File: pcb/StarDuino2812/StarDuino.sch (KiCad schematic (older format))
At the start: 68 parts, among them J1 Screw_Terminal_01x02, Q1 IRLML6401, U1 ATmega328P-AU, Y1 Crystal

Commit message: 2812 star in work
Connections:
- net at U1.7 (XTAL1/PB6): now also C2.1, Y1.2
- net at U1.8 (XTAL2/PB7): now also C1.1, Y1.1
- net at D1.2 (DOUT): now also D5.4 (DIN); no longer D2.4 (DIN)
- net at D1.4 (DIN): now also D10.2 (DOUT)
- net at D2.2 (DOUT): now also D6.4 (DIN); no longer D3.4 (DIN)
- net at D3.2 (DOUT): now also D7.4 (DIN); no longer D4.4 (DIN)
- net at D4.2 (DOUT): now also D8.4 (DIN)
- net at D9.2 (DOUT): no longer D10.4 (DIN)
- net at D9.4 (DIN): now also D5.2 (DOUT)
- net at D11.4 (DIN): now also D7.2 (DOUT); no longer D10.2 (DOUT)
- net at D11.2 (DOUT): now also D2.4 (DIN); no longer D12.4 (DIN)
- net at D12.2 (DOUT): now also D3.4 (DIN)
- net at D17.2 (DOUT): no longer D18.4 (DIN)
- net at D18.2 (DOUT): no longer D19.4 (DIN)
- net at D19.2 (DOUT): no longer D20.4 (DIN)
- net at D25.2 (DOUT): no longer D26.4 (DIN)
- net at D26.2 (DOUT): no longer D27.4 (DIN)
- net at D27.2 (DOUT): no longer D28.4 (DIN)
- net at D33.2 (DOUT): no longer D34.4 (DIN)
- net at D34.2 (DOUT): no longer D35.4 (DIN)
- net at D35.2 (DOUT): no longer D36.4 (DIN)
- net at D41.2 (DOUT): no longer D42.4 (DIN)
- net at D42.2 (DOUT): no longer D43.4 (DIN)
- net at D43.2 (DOUT): no longer D44.4 (DIN)
- net at D49.2 (DOUT): no longer D50.4 (DIN)
- net at D50.2 (DOUT): no longer D51.4 (DIN)
- net at D51.2 (DOUT): no longer D52.4 (DIN)
- net at D57.2 (DOUT): no longer D58.4 (DIN)
- net at D58.2 (DOUT): no longer D59.4 (DIN)
- net at D59.2 (DOUT): no longer D60.4 (DIN)
- net at D6.2 (DOUT): now also D10.4 (DIN); no longer D7.4 (DIN)
- net at D8.2 (DOUT): now also D12.4 (DIN)
- net at D13.2 (DOUT): no longer D14.4 (DIN)
- net at D14.2 (DOUT): no longer D15.4 (DIN)
- net at D15.2 (DOUT): no longer D16.4 (DIN)
- net at D21.2 (DOUT): no longer D22.4 (DIN)
- net at D22.2 (DOUT): no longer D23.4 (DIN)
- net at D23.2 (DOUT): no longer D24.4 (DIN)
- net at D29.2 (DOUT): no longer D30.4 (DIN)
- net at D30.2 (DOUT): no longer D31.4 (DIN)
- net at D31.2 (DOUT): no longer D32.4 (DIN)
- net at D37.2 (DOUT): no longer D38.4 (DIN)
- net at D38.2 (DOUT): no longer D39.4 (DIN)
- net at D39.2 (DOUT): no longer D40.4 (DIN)
- net at D45.2 (DOUT): no longer D46.4 (DIN)
- net at D46.2 (DOUT): no longer D47.4 (DIN)
- net at D47.2 (DOUT): no longer D48.4 (DIN)
- net at D53.2 (DOUT): no longer D54.4 (DIN)
- net at D54.2 (DOUT): no longer D55.4 (DIN)
- net at D55.2 (DOUT): no longer D56.4 (DIN)
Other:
- moved on the sheet: D1, D10, D11, D12, D13, D14, D15, D16, D17, D18, D19, D2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

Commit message: 2812 star in work
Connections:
- net at D9.2 (DOUT): now also D16.4 (DIN)
- net at D17.2 (DOUT): now also D21.4 (DIN)
- net at D17.4 (DIN): now also D13.2 (DOUT)
- net at D18.2 (DOUT): now also D22.4 (DIN)
- net at D18.4 (DIN): now also D14.2 (DOUT)
- net at D19.2 (DOUT): now also D23.4 (DIN)
- net at D19.4 (DIN): now also D15.2 (DOUT)
- net at D20.2 (DOUT): now also D24.4 (DIN)
- net at D20.4 (DIN): now also D16.2 (DOUT)
- net at D25.2 (DOUT): now also D29.4 (DIN)
- net at D25.4 (DIN): now also D34.2 (DOUT)
- net at D26.2 (DOUT): now also D30.4 (DIN)
- net at D26.4 (DIN): now also D35.2 (DOUT)
- net at D27.2 (DOUT): now also D31.4 (DIN)
- net at D27.4 (DIN): now also D36.2 (DOUT)
- net at D28.2 (DOUT): now also D32.4 (DIN)
- net at D28.4 (DIN): now also D21.2 (DOUT)
- net at D33.2 (DOUT): now also D40.4 (DIN)
- net at D33.4 (DIN): now also D29.2 (DOUT)
- net at D34.4 (DIN): now also D30.2 (DOUT)
- net at D35.4 (DIN): now also D31.2 (DOUT)
- net at D36.4 (DIN): now also D32.2 (DOUT)
- net at D41.2 (DOUT): now also D45.4 (DIN)
- net at D41.4 (DIN): now also D37.2 (DOUT)
- net at D42.2 (DOUT): now also D46.4 (DIN)
- net at D42.4 (DIN): now also D38.2 (DOUT)
- net at D43.2 (DOUT): now also D47.4 (DIN)
- net at D43.4 (DIN): now also D39.2 (DOUT)
- net at D44.2 (DOUT): now also D48.4 (DIN)
- net at D44.4 (DIN): now also D40.2 (DOUT)
- net at D49.2 (DOUT): now also D53.4 (DIN)
- net at D49.4 (DIN): now also D58.2 (DOUT)
- net at D50.2 (DOUT): now also D54.4 (DIN)
- net at D50.4 (DIN): now also D59.2 (DOUT)
- net at D51.2 (DOUT): now also D55.4 (DIN)
- net at D51.4 (DIN): now also D60.2 (DOUT)
- net at D52.2 (DOUT): now also D56.4 (DIN)
- net at D52.4 (DIN): now also D45.2 (DOUT)
- net at D57.4 (DIN): now also D53.2 (DOUT)
- net at D58.4 (DIN): now also D54.2 (DOUT)
- net at D59.4 (DIN): now also D55.2 (DOUT)
- net at D60.4 (DIN): now also D56.2 (DOUT)
- net at D13.4 (DIN): now also D22.2 (DOUT)
- net at D14.4 (DIN): now also D23.2 (DOUT)
- net at D15.4 (DIN): now also D24.2 (DOUT)
- net at D37.4 (DIN): now also D46.2 (DOUT)
- net at D38.4 (DIN): now also D47.2 (DOUT)
- net at D39.4 (DIN): now also D48.2 (DOUT)
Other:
- moved on the sheet: H1

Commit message: Almost ready
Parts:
- added C4: 0.1uF, Capacitor_SMD:C_0805_2012Metric_Pad1.18x1.45mm_HandSolder, symbol Device:C
- added H2, H3, H4: MountingHole, MountingHole:MountingHole_2.5mm, symbol Mechanical:MountingHole
- added J2: Conn_01x03_Male, Connector_PinHeader_2.54mm:PinHeader_1x03_P2.54mm_Vertical, symbol Connector:Conn_01x03_Male
- added R1: 1M, Resistor_SMD:R_0805_2012Metric_Pad1.20x1.40mm_HandSolder, symbol Device:R
- added R2: 10k, Resistor_SMD:R_0805_2012Metric_Pad1.20x1.40mm_HandSolder, symbol Device:R
- Y1: value Crystal -> 16M; footprint Crystal:Crystal_SMD_HC49-SD_HandSoldering -> Crystal:Crystal_HC49-4H_Vertical
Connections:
- net GND: now also C4.1
- net VCC: now also U1.18 (AVCC), U1.4 (VCC), U1.6 (VCC), C4.2, R2.1
- net at U1.24 (PC1): now also D4.4 (DIN)
- net ~Reset: now reaches U1.29 (~RESET~/PC6)
- net ~Reset: now also J2.1 (Pin_1), R2.2
- net RX: now reaches U1.30 (PD0)
- net RX: now also J2.2 (Pin_2)
- net TX: now reaches U1.31 (PD1)
- net TX: now also J2.3 (Pin_3)
- net at C2.1, U1.7 (XTAL1/PB6), Y1.2: now also R1.1
- net at C1.1, U1.8 (XTAL2/PB7), Y1.1: now also R1.2
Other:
- moved on the sheet: C1, C2

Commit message: Add fifth hole
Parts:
- added H5: MountingHole, MountingHole:MountingHole_2.5mm, symbol Mechanical:MountingHole
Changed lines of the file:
@@
 Wire Wire Line
 	3525 6250 3100 6250
+$Comp
+L Mechanical:MountingHole H5
+U 1 1 601A7A2A
+P 10850 7225
+F 0 "H5" H 10950 7271 50  0000 L CNN
+F 1 "MountingHole" H 10950 7180 50  0000 L CNN
+F 2 "MountingHole:MountingHole_2.5mm" H 10850 7225 50  0001 C CNN
+F 3 "~" H 10850 7225 50  0001 C CNN
+	1    10850 7225
+	1    0    0    -1
+$EndComp
 $EndSCHEMATC

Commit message: Replace Mounting holes to Mounting pads Add capacitor Add resistors to UART
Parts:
- removed H1, H2, H3, H4, H5: MountingHole, MountingHole:MountingHole_2.5mm, symbol Mechanical:MountingHole
- added C5: 0.1uF, Capacitor_SMD:C_0805_2012Metric_Pad1.18x1.45mm_HandSolder, symbol Device:C
- added C6: 470uF, Capacitor_THT:CP_Axial_L20.0mm_D10.0mm_P26.00mm_Horizontal, symbol Device:CP
- added H10, H6, H7, H8, H9: MountingHole_Pad, MountingHole:MountingHole_2.5mm_Pad_Via, symbol Mechanical:MountingHole_Pad
- added J3: Conn_01x01_Male, Connector_PinHeader_2.54mm:PinHeader_1x01_P2.54mm_Vertical, symbol Connector:Conn_01x01_Male
- added R3, R4: 1k, Resistor_SMD:R_0805_2012Metric_Pad1.20x1.40mm_HandSolder, symbol Device:R
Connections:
- net GND: now also C6.2, J3.1 (Pin_1)
- net RX: now also R3.2; no longer J2.2 (Pin_2)
- net TX: now also R4.2; no longer J2.3 (Pin_3)
- net VCC: now also C6.1
- net ~Reset: now also C5.2; no longer J2.1 (Pin_1)
- new net: C5.1, J2.1 (Pin_1)
- new net: J2.2 (Pin_2), R3.1
- new net: J2.3 (Pin_3), R4.1
- no-connect marks 0 -> 26
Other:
- moved on the sheet: J2
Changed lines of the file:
@@
 Reverse\npolarity\nprotection
-$Comp
-L Mechanical:MountingHole H1
-U 1 1 6027D2D2
-P 10850 5575
-F 0 "H1" H 10950 5621 50  0000 L CNN
-F 1 "MountingHole" H 10950 5530 50  0000 L CNN
-F 2 "MountingHole:MountingHole_2.5mm" H 10850 5575 50  0001 C CNN
-F 3 "~" H 10850 5575 50  0001 C CNN
-	1    10850 5575
-	1    0    0    -1
-$EndComp
 $Comp
 L power:VCC #PWR097
@@
 Wire Wire Line
 	5000 16000 5000 16750
-$Comp
-L Mechanical:MountingHole H2
-U 1 1 60124CA1
-P 10850 5975
-F 0 "H2" H 10950 6021 50  0000 L CNN
-F 1 "MountingHole" H 10950 5930 50  0000 L CNN
-F 2 "MountingHole:MountingHole_2.5mm" H 10850 5975 50  0001 C CNN
-F 3 "~" H 10850 5975 50  0001 C CNN
-	1    10850 5975
-	1    0    0    -1
-$EndComp
-$Comp
-L Mechanical:MountingHole H3
-U 1 1 60125FF8
-P 10850 6375
-F 0 "H3" H 10950 6421 50  0000 L CNN
-F 1 "MountingHole" H 10950 6330 50  0000 L CNN
-F 2 "MountingHole:MountingHole_2.5mm" H 10850 6375 50  0001 C CNN
-F 3 "~" H 10850 6375 50  0001 C CNN
-	1    10850 6375
-	1    0    0    -1
-$EndComp
-$Comp
-L Mechanical:MountingHole H4
-U 1 1 601346AF
-P 10850 6800
-F 0 "H4" H 10950 6846 50  0000 L CNN
-F 1 "MountingHole" H 10950 6755 50  0000 L CNN
-F 2 "MountingHole:MountingHole_2.5mm" H 10850 6800 50  0001 C CNN
-F 3 "~" H 10850 6800 50  0001 C CNN
-	1    10850 6800
-	1    0    0    -1
-$EndComp
 Wire Wire Line
 	2950 4950 3250 4950
@@
 Text Label 3275 6050 0    50   ~ 0
 ~Reset
-Wire Wire Line
-	3200 6050 3525 6050
 Text Label 3275 6150 0    50   ~ 0
 RX
@@
 L Connector:Conn_01x03_Male J2
 U 1 1 60414868
-P 3725 6150
-F 0 "J2" H 3697 6174 50  0000 R CNN
-F 1 "Conn_01x03_Male" H 3697 6083 50  0000 R CNN
-F 2 "Connector_PinHeader_2.54mm:PinHeader_1x03_P2.54mm_Vertical" H 3725 6150 50  0001 C CNN
-F 3 "~" H 3725 6150 50  0001 C CNN
-	1    3725 6150
+P 4350 6150
+F 0 "J2" H 4322 6174 50  0000 R CNN
+F 1 "Conn_01x03_Male" H 4675 5950 50  0000 R CNN
+F 2 "Connector_PinHeader_2.54mm:PinHeader_1x03_P2.54mm_Vertical" H 4350 6150 50  0001 C CNN
+F 3 "~" H 4350 6150 50  0001 C CNN
+	1    4350 6150
 	-1   0    0    -1
 $EndComp
@@
 	3525 6250 3100 6250
 $Comp
-L Mechanical:MountingHole H5
-U 1 1 601A7A2A
-P 10850 7225
-F 0 "H5" H 10950 7271 50  0000 L CNN
-F 1 "MountingHole" H 10950 7180 50  0000 L CNN
-F 2 "MountingHole:MountingHole_2.5mm" H 10850 7225 50  0001 C CNN
-F 3 "~" H 10850 7225 50  0001 C CNN
-	1    10850 7225
-	1    0    0    -1
-$EndComp
+L Device:R R4
+U 1 1 606499DB
+P 3675 6250
+F 0 "R4" V 3625 6075 50  0000 C CNN
+F 1 "1k" V 3675 6250 50  0000 C CNN
+F 2 "Resistor_SMD:R_0805_2012Metric_Pad1.20x1.40mm_HandSolder" V 3605 6250 50  0001 C CNN
+F 3 "~" H 3675 6250 50  0001 C CNN
+	1    3675 6250
+	0    1    1    0
+$EndComp
+$Comp
+L Device:R R3
+U 1 1 6064AD4D
+P 3675 6150
+F 0 "R3" V 3625 5975 50  0000 C CNN
+F 1 "1k" V 3675 6150 50  0000 C CNN
+F 2 "Resistor_SMD:R_0805_2012Metric_Pad1.20x1.40mm_HandSolder" V 3605 6150 50  0001 C CNN
+F 3 "~" H 3675 6150 50  0001 C CNN
+	1    3675 6150
+	0    1    1    0
+$EndComp
+$Comp
+L Device:C C5
+U 1 1 6064C37E
+P 3875 6050
+F 0 "C5" V 3825 5950 50  0000 C CNN
+F 1 "0.1uF" V 3825 6225 50  0000 C CNN
+F 2 "Capacitor_SMD:C_0805_2012Metric_Pad1.18x1.45mm_HandSolder" H 3913 5900 50  0001 C CNN
+F 3 "~" H 3875 6050 50  0001 C CNN
+	1    3875 6050
+	0    1    1    0
+$EndComp
+Wire Wire Line
+	3200 6050 3725 6050
+Wire Wire Line
+	3825 6150 4150 6150
+Wire Wire Line
+	3825 6250 4150 6250
+Wire Wire Line
+	4025 6050 4150 6050
+NoConn ~ 1750 4250
+NoConn ~ 1750 4450
+NoConn ~ 1750 4550
+NoConn ~ 2950 4250
+NoConn ~ 2950 4350
+NoConn ~ 2950 4450
+NoConn ~ 2950 4550
+NoConn ~ 2950 4650
+NoConn ~ 2950 4750
+NoConn ~ 2950 5150
+NoConn ~ 2950 5350
+NoConn ~ 2950 5450
+NoConn ~ 2950 5550
+NoConn ~ 2950 5650
+NoConn ~ 2950 6150
+NoConn ~ 2950 6250
+NoConn ~ 2950 6350
+NoConn ~ 2950 6450
+NoConn ~ 2950 6550
+NoConn ~ 2950 6650
+NoConn ~ 9350 18750
+$Comp
+L Mechanical:MountingHole_Pad H6
+U 1 1 60810FD8
+P 12250 5550
+F 0 "H6" H 12350 5599 50  0000 L CNN
+F 1 "MountingHole_Pad" H 12350 5508 50  0000 L CNN
+F 2 "MountingHole:MountingHole_2.5mm_Pad_Via" H 12250 5550 50  0001 C CNN
+F 3 "~" H 12250 5550 50  0001 C CNN
+	1    12250 5550
+	1    0    0    -1
+$EndComp
+$Comp
+L Mechanical:MountingHole_Pad H7
+U 1 1 60812577
+P 12250 6050
+F 0 "H7" H 12350 6099 50  0000 L CNN
+F 1 "MountingHole_Pad" H 12350 6008 50  0000 L CNN
+F 2 "MountingHole:MountingHole_2.5mm_Pad_Via" H 12250 6050 50  0001 C CNN
+F 3 "~" H 12250 6050 50  0001 C CNN
+	1    12250 6050
+	1    0    0    -1
+$EndComp
+$Comp
+L Mechanical:MountingHole_Pad H8
+U 1 1 60812E0D
+P 12250 6550
+F 0 "H8" H 12350 6599 50  0000 L CNN
+F 1 "MountingHole_Pad" H 12350 6508 50  0000 L CNN
+F 2 "MountingHole:MountingHole_2.5mm_Pad_Via" H 12250 6550 50  0001 C CNN
+F 3 "~" H 12250 6550 50  0001 C CNN
+	1    12250 6550
+	1    0    0    -1
+$EndComp
+$Comp
+L Mechanical:MountingHole_Pad H9
+U 1 1 608149CE
+P 12250 7050
+F 0 "H9" H 12350 7099 50  0000 L CNN
+F 1 "MountingHole_Pad" H 12350 7008 50  0000 L CNN
+F 2 "MountingHole:MountingHole_2.5mm_Pad_Via" H 12250 7050 50  0001 C CNN
+F 3 "~" H 12250 7050 50  0001 C CNN
+	1    12250 7050
+	1    0    0    -1
+$EndComp
+$Comp
+L Mechanical:MountingHole_Pad H10
+U 1 1 60814E06
+P 12250 7550
+F 0 "H10" H 12350 7599 50  0000 L CNN
+F 1 "MountingHole_Pad" H 12350 7508 50  0000 L CNN
+F 2 "MountingHole:MountingHole_2.5mm_Pad_Via" H 12250 7550 50  0001 C CNN
+F 3 "~" H 12250 7550 50  0001 C CNN
+	1    12250 7550
+	1    0    0    -1
+$EndComp
+NoConn ~ 12250 5650
+NoConn ~ 12250 6150
+NoConn ~ 12250 6650
+NoConn ~ 12250 7150
+NoConn ~ 12250 7650
+$Comp
+L Device:CP C6
+U 1 1 6094EE0B
+P 3000 7900
+F 0 "C6" H 3118 7946 50  0000 L CNN
+F 1 "470uF" H 3118 7855 50  0000 L CNN
+F 2 "Capacitor_THT:CP_Axial_L20.0mm_D10.0mm_P26.00mm_Horizontal" H 3038 7750 50  0001 C CNN
+F 3 "~" H 3000 7900 50  0001 C CNN
+	1    3000 7900
+	1    0    0    -1
+$EndComp
+$Comp
+L power:VCC #PWR0129
+U 1 1 60950781
+P 3000 7750
+F 0 "#PWR0129" H 3000 7600 50  0001 C CNN
+F 1 "VCC" H 3015 7923 50  0000 C CNN
+F 2 "" H 3000 7750 50  0001 C CNN
+F 3 "" H 3000 7750 50  0001 C CNN
+	1    3000 7750
+	1    0    0    -1
+$EndComp
+$Comp
+L power:GND #PWR0134
+U 1 1 60951E6F
+P 3000 8050
+F 0 "#PWR0134" H 3000 7800 50  0001 C CNN
+F 1 "GND" H 3005 7877 50  0000 C CNN
+F 2 "" H 3000 8050 50  0001 C CNN
+F 3 "" H 3000 8050 50  0001 C CNN
+	1    3000 8050
+	1    0    0    -1
+$EndComp
+$Comp
+L Connector:Conn_01x01_Male J3
+U 1 1 609AFD54
+P 4350 6700
+F 0 "J3" H 4322 6724 50  0000 R CNN
+F 1 "Conn_01x01_Male" H 4675 6850 50  0000 R CNN
+F 2 "Connector_PinHeader_2.54mm:PinHeader_1x01_P2.54mm_Vertical" H 4350 6700 50  0001 C CNN
+F 3 "~" H 4350 6700 50  0001 C CNN
+	1    4350 6700
+	-1   0    0    -1
+$EndComp
+$Comp
+L power:GND #PWR0135
+U 1 1 609DAEB4
+P 4150 6700
+F 0 "#PWR0135" H 4150 6450 50  0001 C CNN
+F 1 "GND" H 4155 6527 50  0000 C CNN
+F 2 "" H 4150 6700 50  0001 C CNN
+F 3 "" H 4150 6700 50  0001 C CNN
+	1    4150 6700
+	1    0    0    -1
+$EndComp

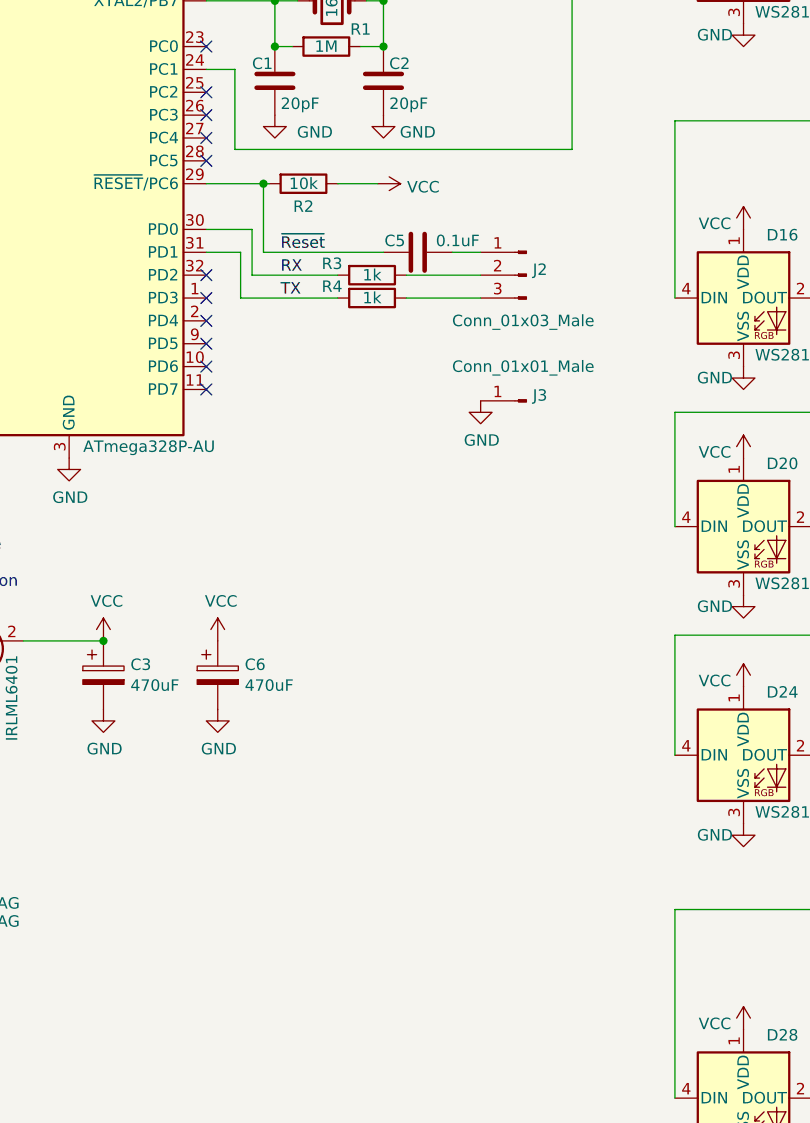
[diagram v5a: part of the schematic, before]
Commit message: Polishing. Add resistor, silk, etc
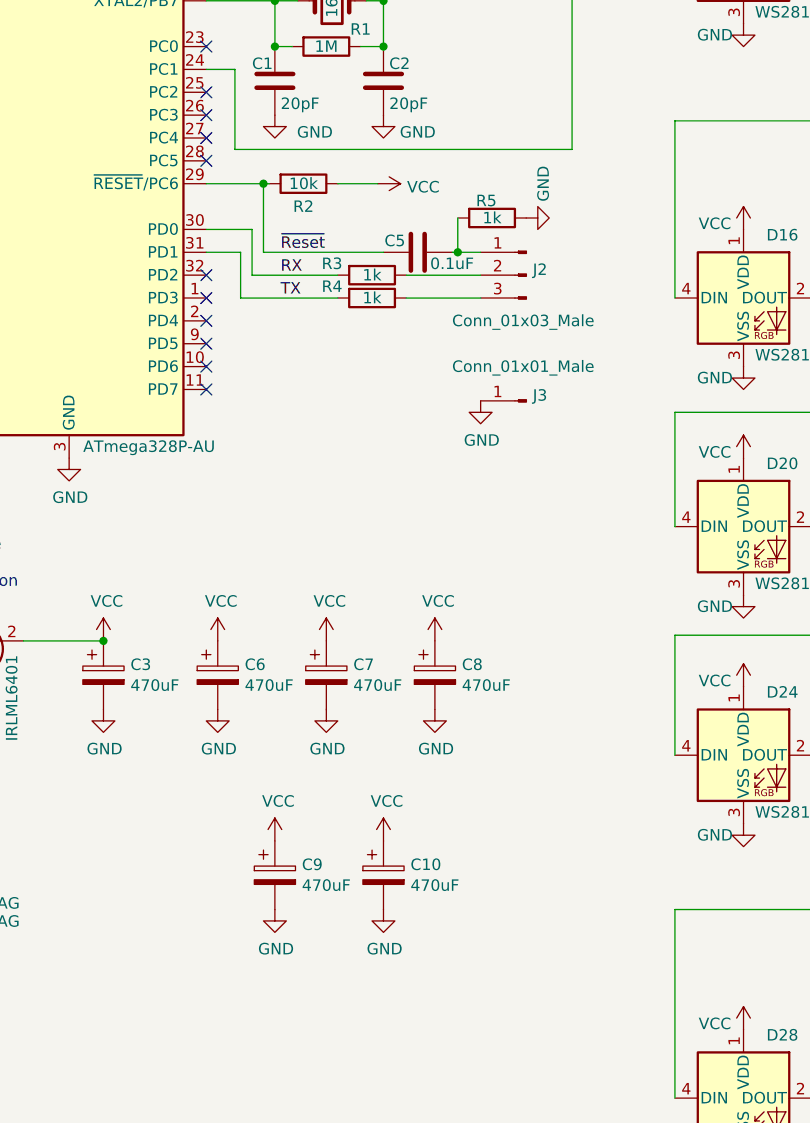
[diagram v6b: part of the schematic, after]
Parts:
- added C10, C7, C8, C9: 470uF, Capacitor_THT:CP_Axial_L20.0mm_D10.0mm_P26.00mm_Horizontal, symbol Device:CP
- added R5: 1k, Resistor_SMD:R_0805_2012Metric_Pad1.20x1.40mm_HandSolder, symbol Device:R
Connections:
- net GND: now also C10.2, C7.2, C8.2, C9.2, R5.1
- net VCC: now also C10.1, C7.1, C8.1, C9.1
- net at C5.1, J2.1 (Pin_1): now also R5.2
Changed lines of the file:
@@
 P 3875 6050
 F 0 "C5" V 3825 5950 50  0000 C CNN
-F 1 "0.1uF" V 3825 6225 50  0000 C CNN
+F 1 "0.1uF" V 3925 6200 50  0000 C CNN
 F 2 "Capacitor_SMD:C_0805_2012Metric_Pad1.18x1.45mm_HandSolder" H 3913 5900 50  0001 C CNN
 F 3 "~" H 3875 6050 50  0001 C CNN
@@
 	3825 6250 4150 6250
 Wire Wire Line
-	4025 6050 4150 6050
+	4025 6050 4050 6050
 NoConn ~ 1750 4250
 NoConn ~ 1750 4450
@@
 	1    0    0    -1
 $EndComp
+$Comp
+L Device:CP C7
+U 1 1 6065C492
+P 3475 7900
+F 0 "C7" H 3593 7946 50  0000 L CNN
+F 1 "470uF" H 3593 7855 50  0000 L CNN
+F 2 "Capacitor_THT:CP_Axial_L20.0mm_D10.0mm_P26.00mm_Horizontal" H 3513 7750 50  0001 C CNN
+F 3 "~" H 3475 7900 50  0001 C CNN
+	1    3475 7900
+	1    0    0    -1
+$EndComp
+$Comp
+L power:VCC #PWR0136
+U 1 1 6065C498
+P 3475 7750
+F 0 "#PWR0136" H 3475 7600 50  0001 C CNN
+F 1 "VCC" H 3490 7923 50  0000 C CNN
+F 2 "" H 3475 7750 50  0001 C CNN
+F 3 "" H 3475 7750 50  0001 C CNN
+	1    3475 7750
+	1    0    0    -1
+$EndComp
+$Comp
+L power:GND #PWR0138
+U 1 1 6065C49E
+P 3475 8050
+F 0 "#PWR0138" H 3475 7800 50  0001 C CNN
+F 1 "GND" H 3480 7877 50  0000 C CNN
+F 2 "" H 3475 8050 50  0001 C CNN
+F 3 "" H 3475 8050 50  0001 C CNN
+	1    3475 8050
+	1    0    0    -1
+$EndComp
+$Comp
+L Device:CP C8
+U 1 1 6066952F
+P 3950 7900
+F 0 "C8" H 4068 7946 50  0000 L CNN
+F 1 "470uF" H 4068 7855 50  0000 L CNN
+F 2 "Capacitor_THT:CP_Axial_L20.0mm_D10.0mm_P26.00mm_Horizontal" H 3988 7750 50  0001 C CNN
+F 3 "~" H 3950 7900 50  0001 C CNN
+	1    3950 7900
+	1    0    0    -1
+$EndComp
+$Comp
+L power:VCC #PWR0137
+U 1 1 60669535
+P 3950 7750
+F 0 "#PWR0137" H 3950 7600 50  0001 C CNN
+F 1 "VCC" H 3965 7923 50  0000 C CNN
+F 2 "" H 3950 7750 50  0001 C CNN
+F 3 "" H 3950 7750 50  0001 C CNN
+	1    3950 7750
+	1    0    0    -1
+$EndComp
+$Comp
+L power:GND #PWR0139
+U 1 1 6066953B
+P 3950 8050
+F 0 "#PWR0139" H 3950 7800 50  0001 C CNN
+F 1 "GND" H 3955 7877 50  0000 C CNN
+F 2 "" H 3950 8050 50  0001 C CNN
+F 3 "" H 3950 8050 50  0001 C CNN
+	1    3950 8050
+	1    0    0    -1
+$EndComp
+$Comp
+L Device:CP C9
+U 1 1 606798AE
+P 3250 8775
+F 0 "C9" H 3368 8821 50  0000 L CNN
+F 1 "470uF" H 3368 8730 50  0000 L CNN
+F 2 "Capacitor_THT:CP_Axial_L20.0mm_D10.0mm_P26.00mm_Horizontal" H 3288 8625 50  0001 C CNN
+F 3 "~" H 3250 8775 50  0001 C CNN
+	1    3250 8775
+	1    0    0    -1
+$EndComp
+$Comp
+L power:VCC #PWR0140
+U 1 1 606798B4
+P 3250 8625
+F 0 "#PWR0140" H 3250 8475 50  0001 C CNN
+F 1 "VCC" H 3265 8798 50  0000 C CNN
+F 2 "" H 3250 8625 50  0001 C CNN
+F 3 "" H 3250 8625 50  0001 C CNN
+	1    3250 8625
+	1    0    0    -1
+$EndComp
+$Comp
+L power:GND #PWR0142
+U 1 1 606798BA
+P 3250 8925
+F 0 "#PWR0142" H 3250 8675 50  0001 C CNN
+F 1 "GND" H 3255 8752 50  0000 C CNN
+F 2 "" H 3250 8925 50  0001 C CNN
+F 3 "" H 3250 8925 50  0001 C CNN
+	1    3250 8925
+	1    0    0    -1
+$EndComp
+$Comp
+L Device:CP C10
+U 1 1 606798C0
+P 3725 8775
+F 0 "C10" H 3843 8821 50  0000 L CNN
+F 1 "470uF" H 3843 8730 50  0000 L CNN
+F 2 "Capacitor_THT:CP_Axial_L20.0mm_D10.0mm_P26.00mm_Horizontal" H 3763 8625 50  0001 C CNN
+F 3 "~" H 3725 8775 50  0001 C CNN
+	1    3725 8775
+	1    0    0    -1
+$EndComp
+$Comp
+L power:VCC #PWR0141
+U 1 1 606798C6
+P 3725 8625
+F 0 "#PWR0141" H 3725 8475 50  0001 C CNN
+F 1 "VCC" H 3740 8798 50  0000 C CNN
+F 2 "" H 3725 8625 50  0001 C CNN
+F 3 "" H 3725 8625 50  0001 C CNN
+	1    3725 8625
+	1    0    0    -1
+$EndComp
+$Comp
+L power:GND #PWR0143
+U 1 1 606798CC
+P 3725 8925
+F 0 "#PWR0143" H 3725 8675 50  0001 C CNN
+F 1 "GND" H 3730 8752 50  0000 C CNN
+F 2 "" H 3725 8925 50  0001 C CNN
+F 3 "" H 3725 8925 50  0001 C CNN
+	1    3725 8925
+	1    0    0    -1
+$EndComp
+$Comp
+L Device:R R5
+U 1 1 607223F8
+P 4200 5900
+F 0 "R5" V 4125 5875 50  0000 C CNN
+F 1 "1k" V 4200 5900 50  0000 C CNN
+F 2 "Resistor_SMD:R_0805_2012Metric_Pad1.20x1.40mm_HandSolder" V 4130 5900 50  0001 C CNN
+F 3 "~" H 4200 5900 50  0001 C CNN
+	1    4200 5900
+	0    1    1    0
+$EndComp
+$Comp
+L power:GND #PWR0144
+U 1 1 607240BD
+P 4350 5900
+F 0 "#PWR0144" H 4350 5650 50  0001 C CNN
+F 1 "GND" H 4500 5825 50  0000 C CNN
+F 2 "" H 4350 5900 50  0001 C CNN
+F 3 "" H 4350 5900 50  0001 C CNN
+	1    4350 5900
+	0    -1   -1   0
+$EndComp
+Wire Wire Line
+	4050 5900 4050 6050
+Connection ~ 4050 6050
+Wire Wire Line
+	4050 6050 4150 6050
 $EndSCHEMATC
